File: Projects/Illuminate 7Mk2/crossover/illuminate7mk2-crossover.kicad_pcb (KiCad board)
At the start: 2 copper layers, 144.5 x 110 mm, 27 parts, among them J1 IN (amp), J2 TWEETER, J3 WOOFER

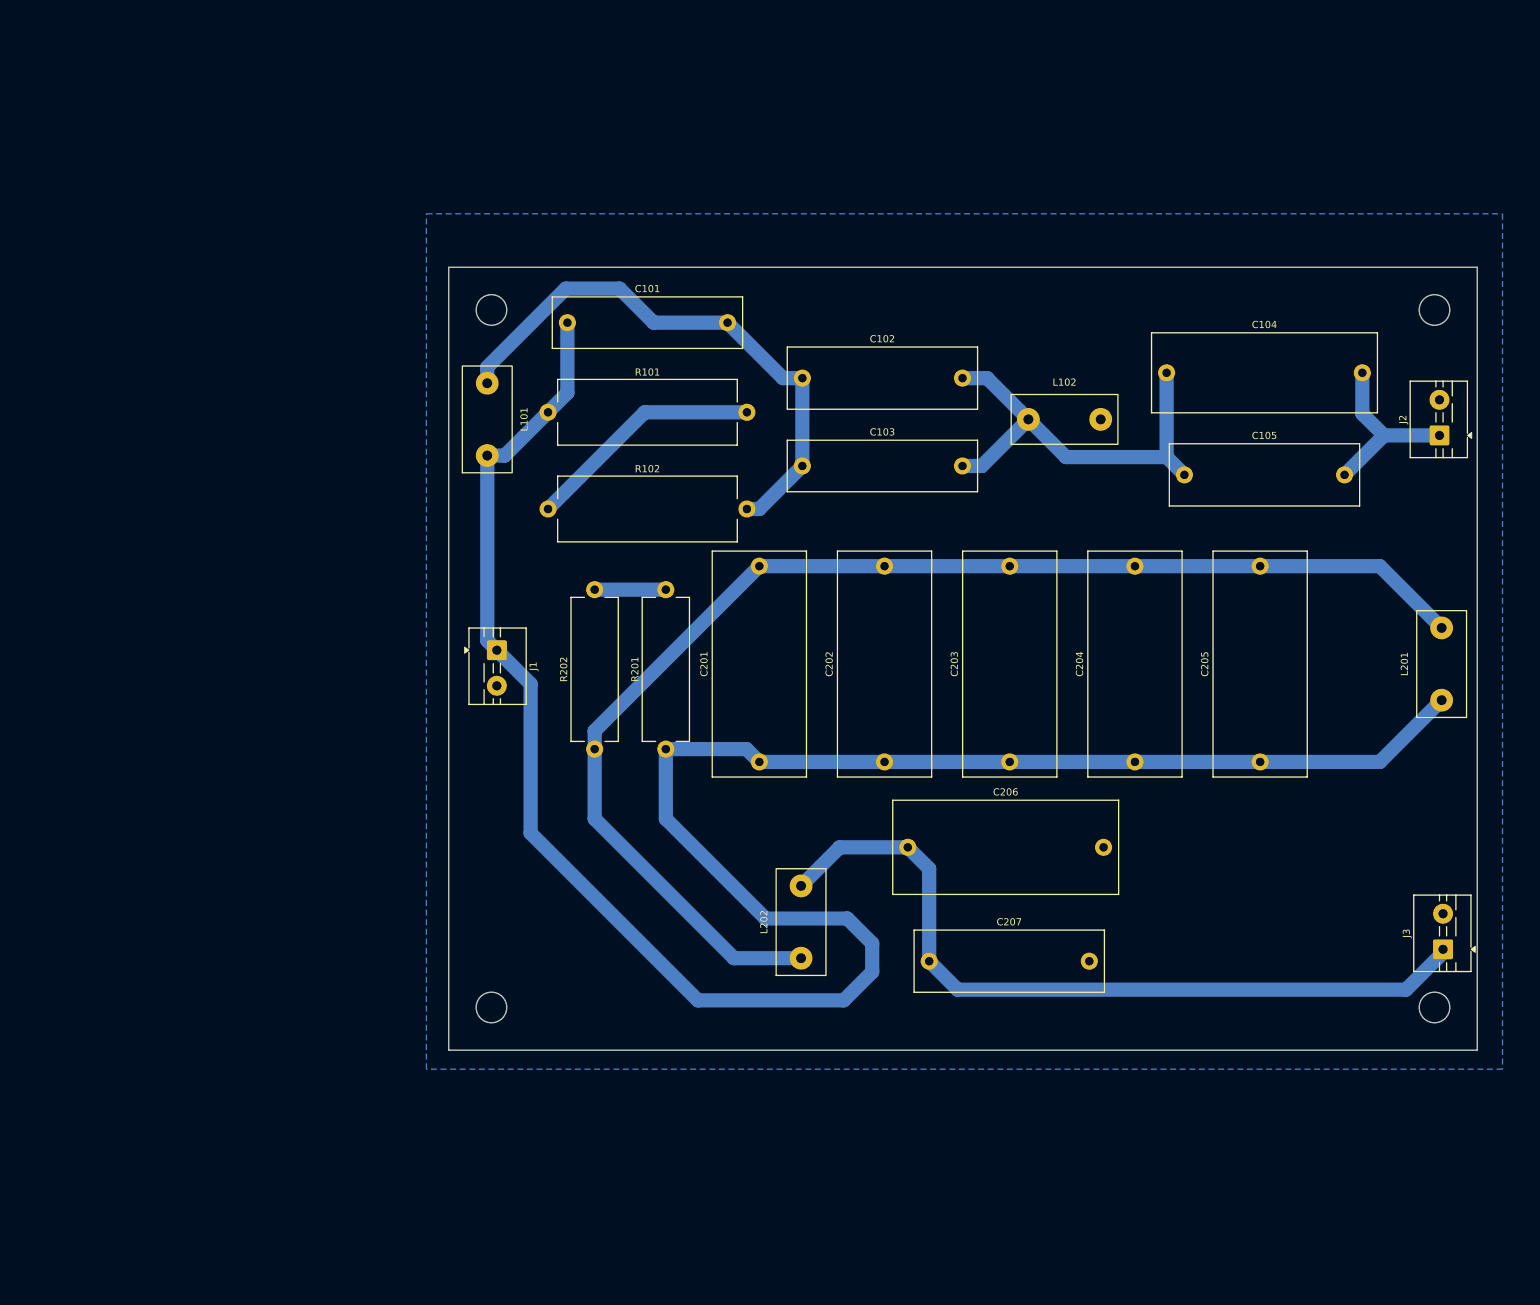
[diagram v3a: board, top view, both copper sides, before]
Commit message: final crosover pcb layout, milled and assembled
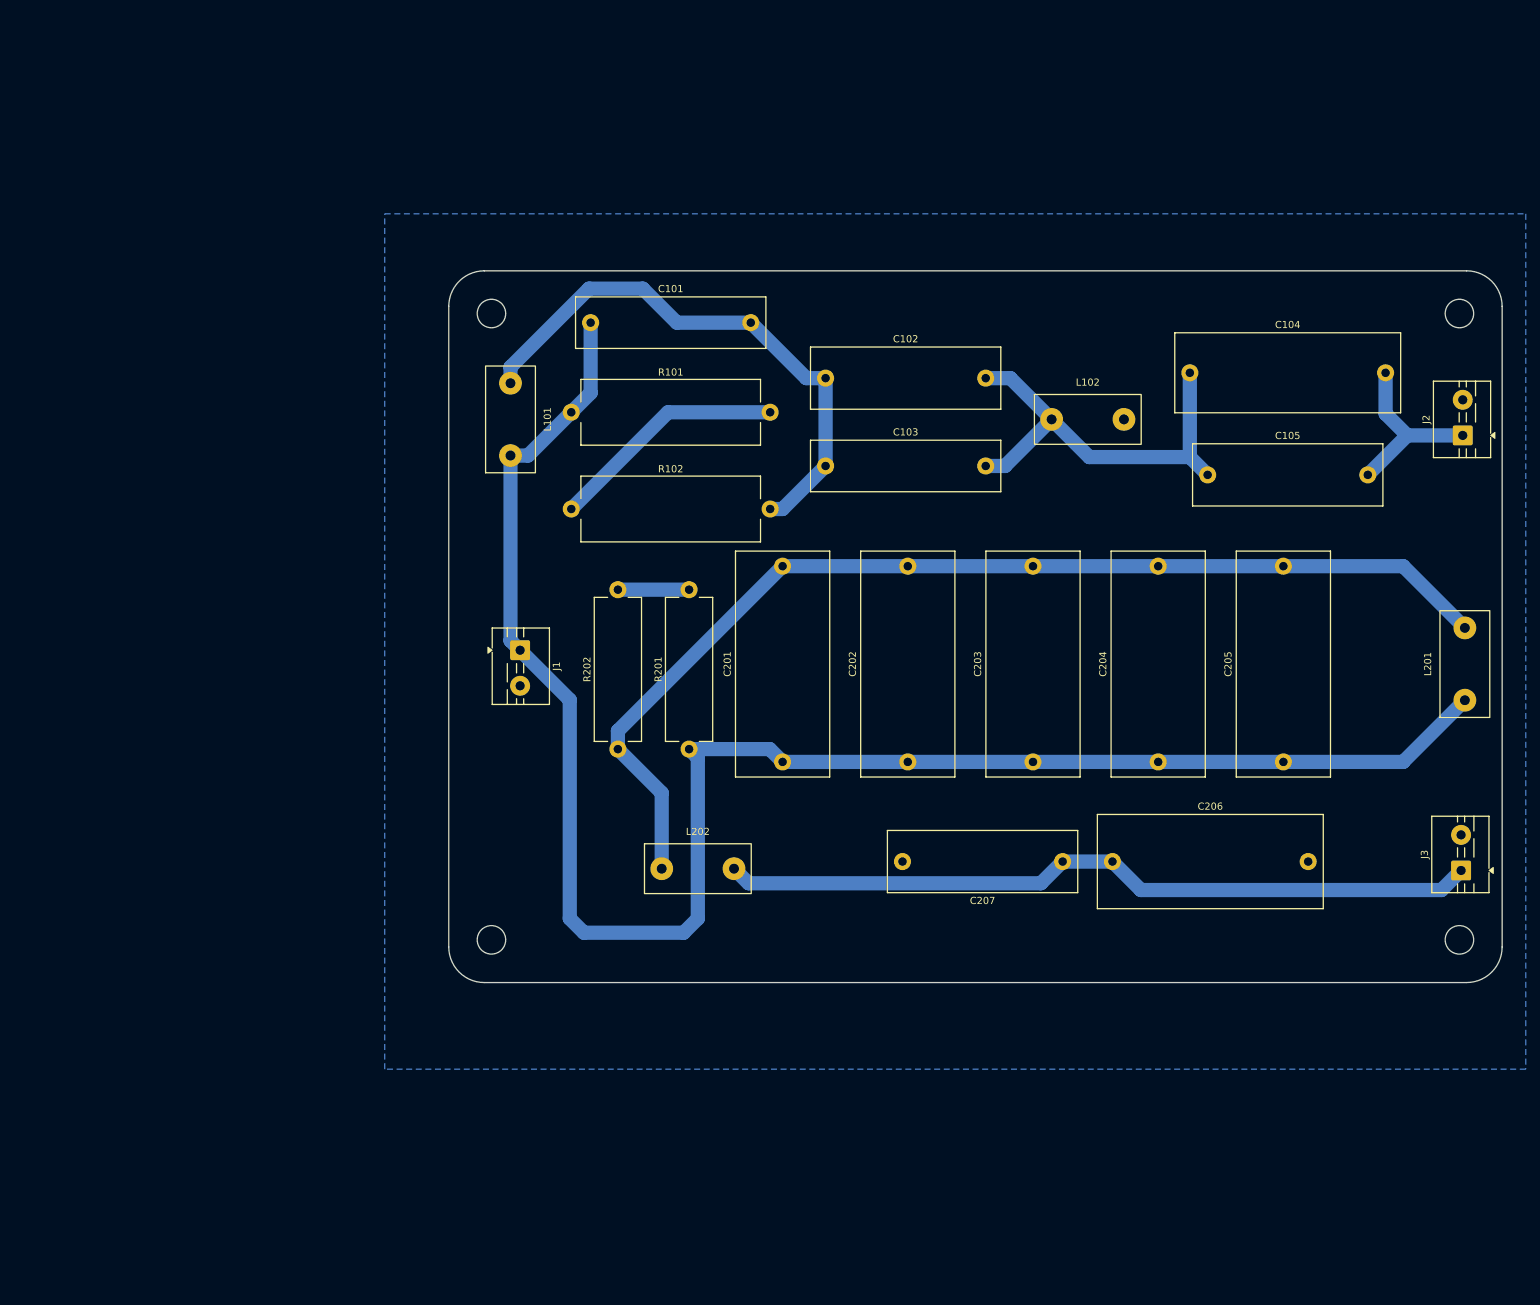
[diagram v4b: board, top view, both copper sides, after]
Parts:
- removed H1, H2, H3, H4: M4, MountingHole_4.3mm_M4_DIN965
- added REF**: MountingHole_4mm, MountingHole:MountingHole_4mm, F.Cu at (67.0, 42.0)
- added REF**: MountingHole_4mm, MountingHole:MountingHole_4mm, F.Cu at (67.0, 130.0)
- added REF**: MountingHole_4mm, MountingHole:MountingHole_4mm, F.Cu at (203.0, 42.0)
- added REF**: MountingHole_4mm, MountingHole:MountingHole_4mm, F.Cu at (203.0, 130.0)
- moved C206 28.8 mm to (154.2, 119.0)
- moved C207 23.4 mm to (147.2, 119.0), turned to 180 degrees
- moved L202 16.3 mm to (96.0, 120.0), turned to 0 degrees
- moved J3 11.4 mm to (203.2, 120.2)
- moved C203 3.26 mm to (143.1, 105.0)
- moved C204 3.26 mm to (160.7, 105.0)
- moved J2 3.26 mm to (203.5, 59.1)
- moved C101 3.26 mm to (80.9, 43.3)
- moved C201 3.26 mm to (107.9, 105.0)
- moved C202 3.26 mm to (125.5, 105.0)
- moved J1 3.26 mm to (71.0, 89.3)
- moved L101 3.26 mm to (69.7, 56.9)
- moved R101 3.26 mm to (78.2, 55.9)
- moved R102 3.26 mm to (78.2, 69.5)
- moved R201 3.26 mm to (94.8, 103.2)
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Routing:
- net /IN+: track 303.1 -> 250.6 mm
- net /WF_C: track 181.6 -> 154.1 mm
- net /WF_D: track 111.0 -> 107.1 mm
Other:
- board size 144.5 x 110 mm -> 148 x 100 mm
